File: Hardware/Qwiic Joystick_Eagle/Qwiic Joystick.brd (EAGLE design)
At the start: 25.4 x 50.8 mm, 41 parts, among them J6 AVR_SPI_PROG_3X2TESTPOINTS, U2 ATTINY85

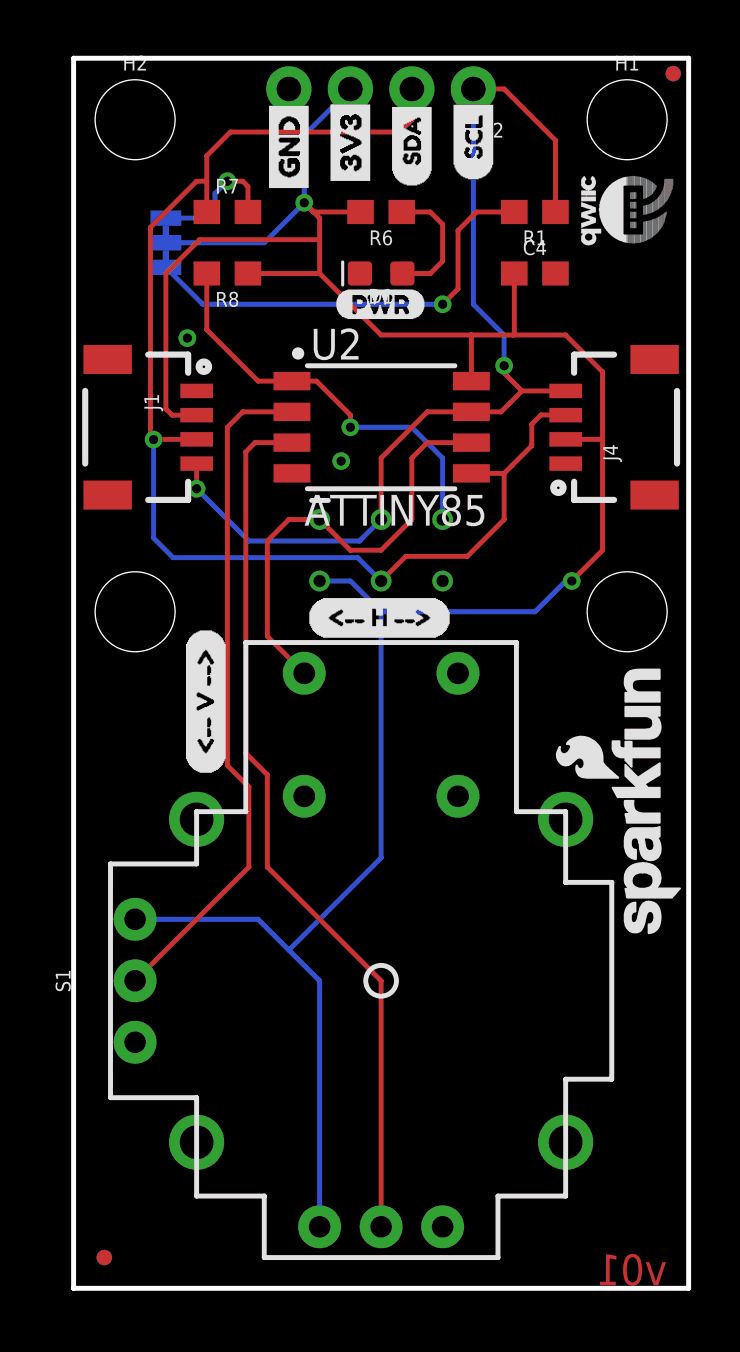
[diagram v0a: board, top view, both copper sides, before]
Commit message: updating buzzard labels to include fatter arrows
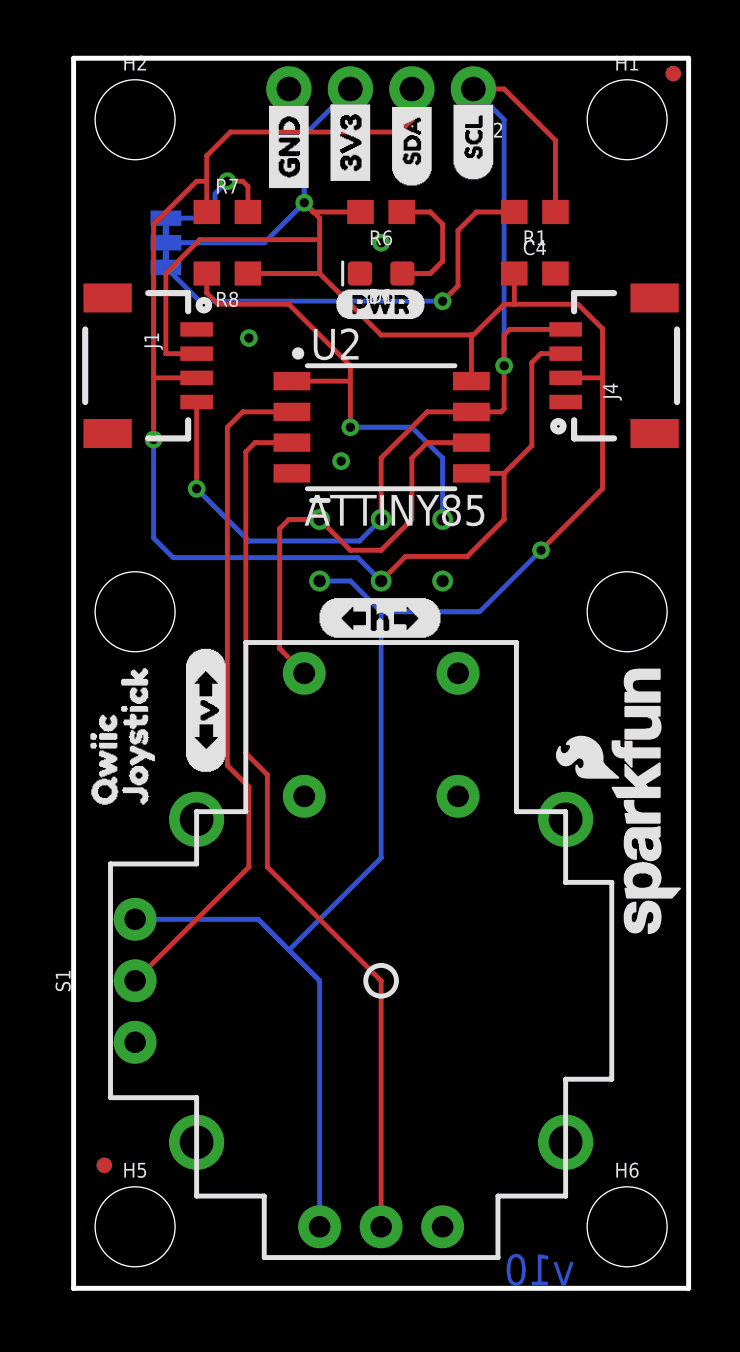
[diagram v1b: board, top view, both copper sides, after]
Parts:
- removed U$22: (no value), Labels:QWIIC-LOGO-SMALL
- added H5, H6: STAND-OFF, SparkFun-Hardware:STAND-OFF
- added U$3: (no value), buzzard_labels (19):QWIIC0
- U$10: device Labels:QWIIC-LOGO-SMALL -> buzzard_labels (20):JOYSTICK0
- U$13: device buzzard_labels (18):QWIIC_JOYSTIIC0 -> buzzard_labels (20):QWIIC_JOYSTICK1
- U$15: device buzzard_labels (1):###_H_###1 -> buzzard_labels (22):##H##0
- U$7: device buzzard_labels (1):###_V_###0 -> buzzard_labels (22):##V##1
- moved U$10 32.5 mm to (2.54, 19.1), flipped to the top, turned to 90 degrees
- moved LOGO1 12.7 mm to (16.5, 12.7)
- moved JP2 3.81 mm to (1.27, 5.08)
- moved JP3 3.81 mm to (1.27, 5.08)
- moved J1 2.54 mm to (5.08, 38.1)
- moved J4 2.54 mm to (20.3, 38.1)
- moved U$15 0.38 mm to (10.0, 27.7)
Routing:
- net SCL: track 41.8 -> 45.8 mm
- net 3.3V: track 108.8 -> 105.7 mm
- net !RST: track 17.1 -> 19.8 mm
- net SDA: track 54.0 -> 56.5 mm
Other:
- board text added: "v10"
- board text removed: "v01"

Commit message: updating resistor values
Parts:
- R1, R7: value 2.2K -> 2.2k
- R8: value 10K -> 10k
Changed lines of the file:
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@@
 <?xml version="1.0" encoding="utf-8"?>
 <!DOCTYPE eagle SYSTEM "eagle.dtd">
-<eagle version="9.1.2">
+<eagle version="9.1.0">
 <drawing>
 <settings>
@@
 <element name="LOGO1" library="SparkFun-Aesthetics" package="OSHW-LOGO-MINI" value="OSHW-LOGOMINI" x="16.51" y="12.7" rot="MR270"/>
 <element name="LOGO2" library="SparkFun-Aesthetics" package="REVISION" value="REVISION" x="-1.27" y="-15.24"/>
-<element name="R1" library="SparkFun-Resistors" package="0603" value="2.2K" x="19.05" y="44.45" rot="R180">
+<element name="R1" library="SparkFun-Resistors" package="0603" value="2.2k" x="19.05" y="44.45" rot="R180">
 <attribute name="NAME" x="19.05" y="43.688" size="0.6096" layer="25" font="vector" ratio="20" rot="R180" align="bottom-center"/>
-<attribute name="PROD_ID" value="RES-07857" x="19.05" y="44.45" size="1.778" layer="27" rot="R180" display="off"/>
-<attribute name="VALUE" x="19.05" y="45.212" size="0.6096" layer="27" font="vector" ratio="20" rot="R180" align="top-center"/>
+<attribute name="PROD_ID" value="RES-08272" x="19.05" y="44.45" size="1.778" layer="27" rot="R180" display="off"/>
+<attribute name="VALUE" value="2.2k" x="19.05" y="45.212" size="0.6096" layer="27" font="vector" ratio="20" rot="R180" align="top-center"/>
 </element>
 <element name="R6" library="SparkFun-Resistors" package="0603" value="1k" x="12.7" y="44.45" rot="R180">
@@
 <attribute name="VALUE" x="12.7" y="45.212" size="0.6096" layer="27" font="vector" ratio="20" rot="R180" align="top-center"/>
 </element>
-<element name="R7" library="SparkFun-Resistors" package="0603" value="2.2K" x="6.35" y="44.45">
+<element name="R7" library="SparkFun-Resistors" package="0603" value="2.2k" x="6.35" y="44.45">
 <attribute name="NAME" x="6.35" y="45.212" size="0.6096" layer="25" font="vector" ratio="20" align="bottom-center"/>
-<attribute name="PROD_ID" value="RES-07857" x="6.35" y="44.45" size="1.778" layer="27" display="off"/>
-<attribute name="VALUE" x="6.35" y="43.688" size="0.6096" layer="27" font="vector" ratio="20" align="top-center"/>
-</element>
-<element name="R8" library="SparkFun-Resistors" package="0603" value="10K" x="6.35" y="41.91" rot="R180">
+<attribute name="PROD_ID" value="RES-08272" x="6.35" y="44.45" size="1.778" layer="27" display="off"/>
+<attribute name="VALUE" value="2.2k" x="6.35" y="43.688" size="0.6096" layer="27" font="vector" ratio="20" align="top-center"/>
+</element>
+<element name="R8" library="SparkFun-Resistors" package="0603" value="10k" x="6.35" y="41.91" rot="R180">
 <attribute name="NAME" x="6.35" y="41.148" size="0.6096" layer="25" font="vector" ratio="20" rot="R180" align="bottom-center"/>
-<attribute name="PROD_ID" value="RES-00818" x="6.35" y="41.91" size="1.778" layer="27" rot="R180" display="off"/>
-<attribute name="VALUE" x="6.35" y="42.672" size="0.6096" layer="27" font="vector" ratio="20" rot="R180" align="top-center"/>
+<attribute name="PROD_ID" value="RES-00824" x="6.35" y="41.91" size="1.778" layer="27" rot="R180" display="off"/>
+<attribute name="VALUE" value="10k" x="6.35" y="42.672" size="0.6096" layer="27" font="vector" ratio="20" rot="R180" align="top-center"/>
 </element>
 <element name="S1" library="SparkFun-Switches" package="JOYSTICK" value="JOYSTICK_THUMB" x="12.7" y="12.7">
